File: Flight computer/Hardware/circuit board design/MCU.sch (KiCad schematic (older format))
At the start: 27 parts, among them J1 Conn_01x04, J2 Conn_01x02, J5 USB_B_Micro, U11 ATSAML21J18B-MUT, U7 W74M64FV, Y2 32.768KHz, Y3 16MHz

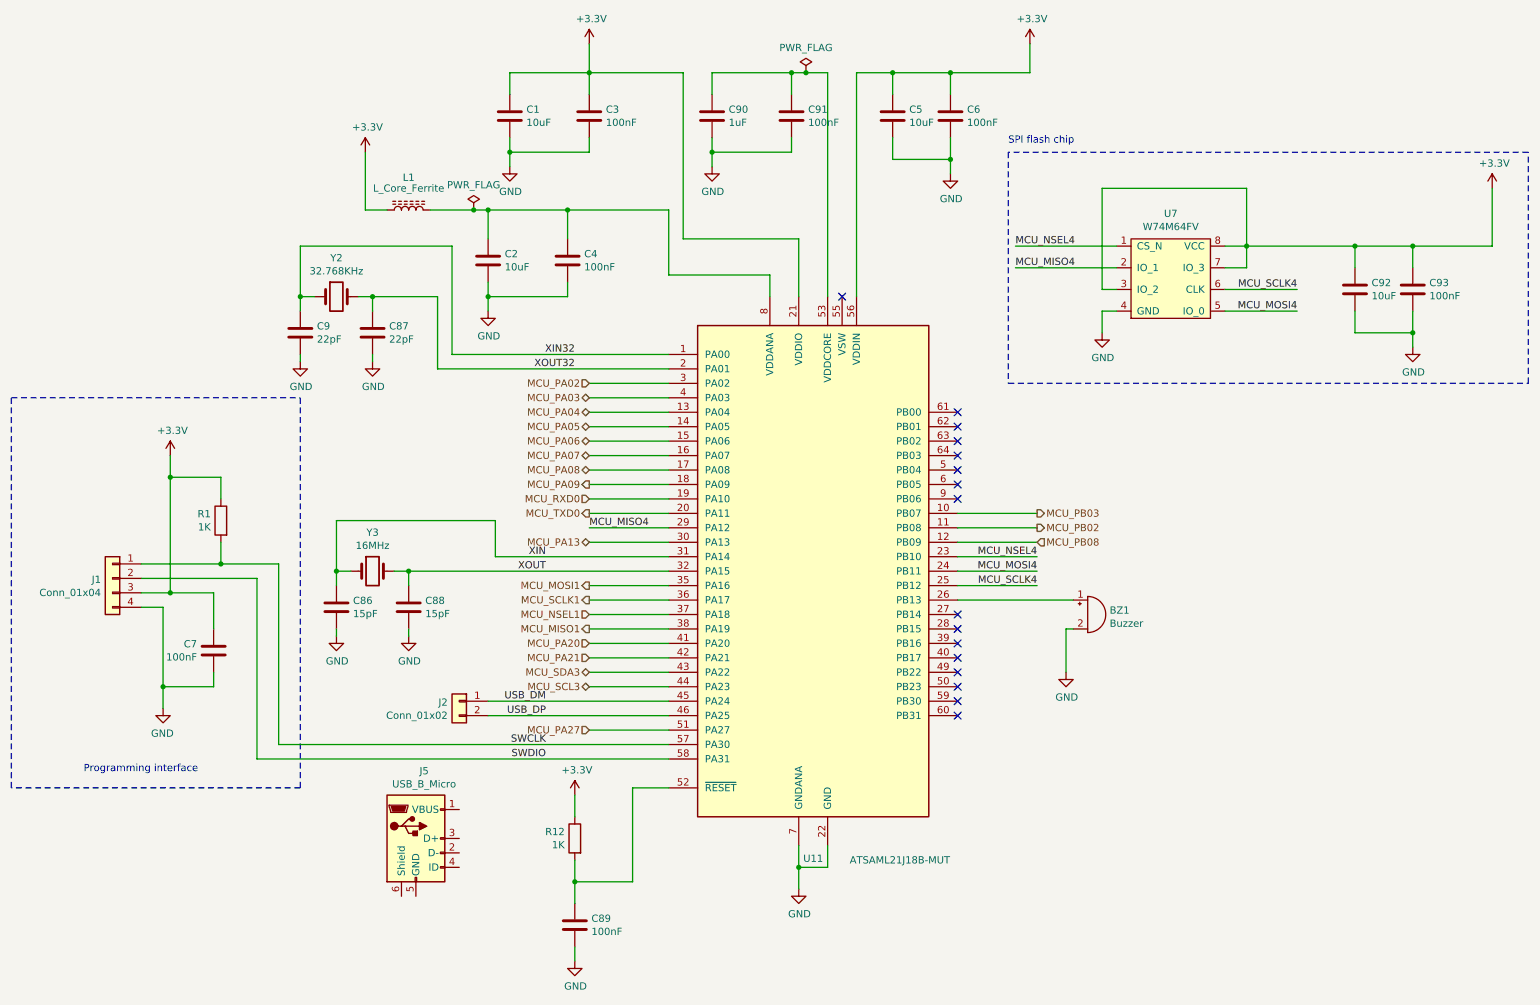
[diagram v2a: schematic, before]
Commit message: put in the IIS2MDC magnetometer
-fixed the error  spi connection pins for Flash chip
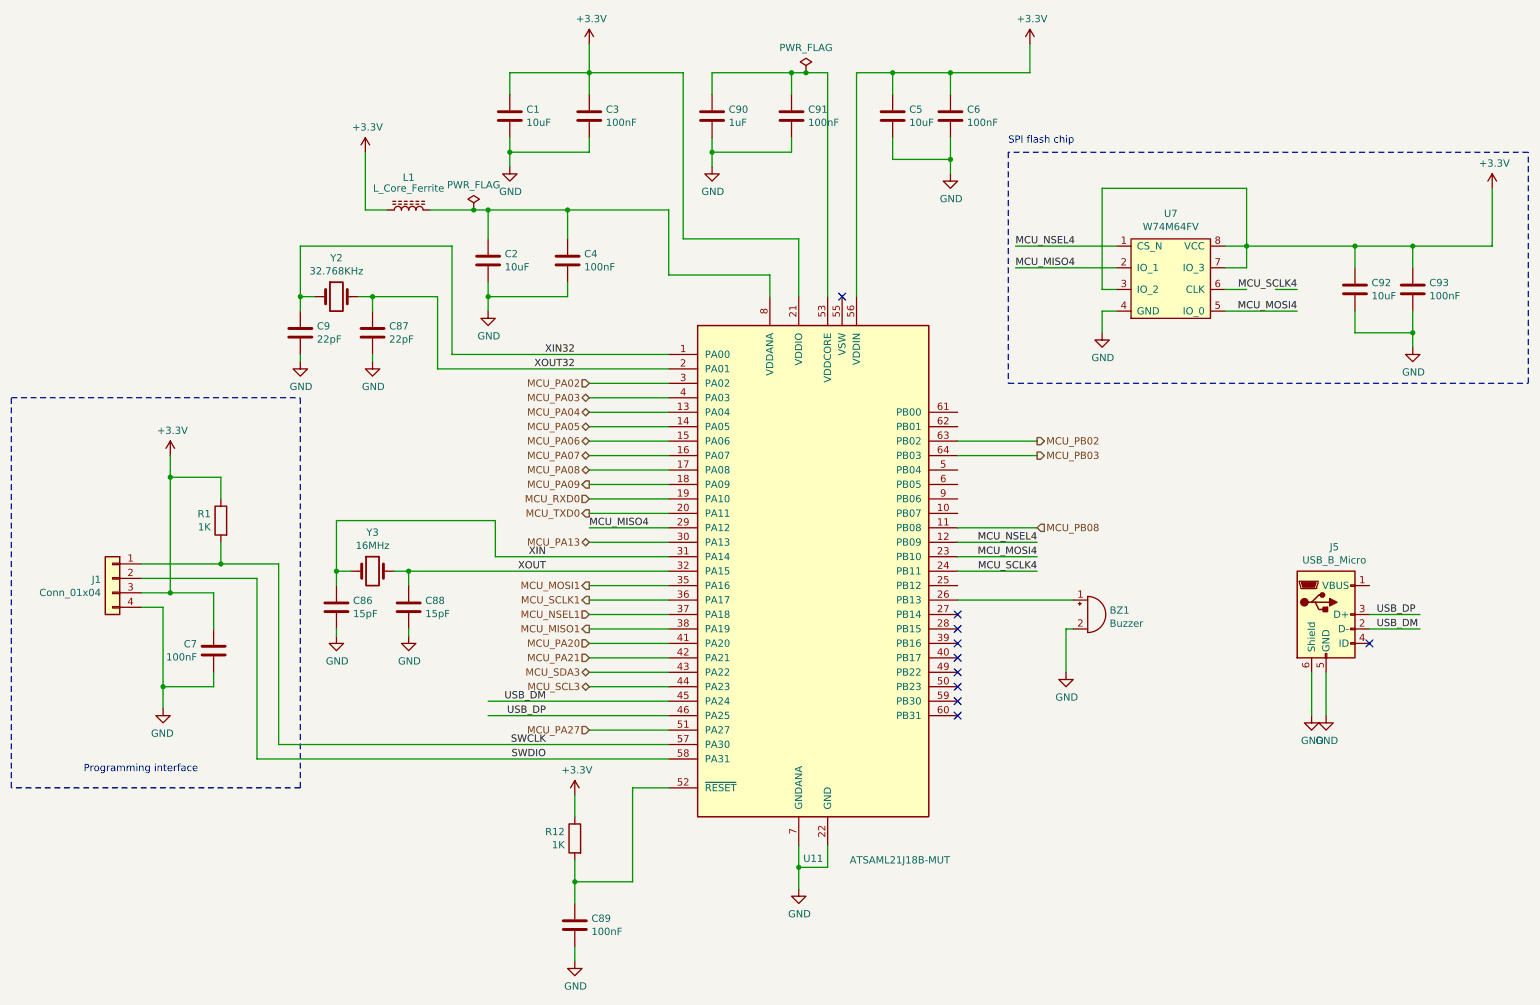
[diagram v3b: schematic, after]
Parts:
- removed J2: Conn_01x02, Connector_PinHeader_1.00mm:PinHeader_1x02_P1.00mm_Vertical, symbol Connector_Generic:Conn_01x02
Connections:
- wire segments 158 -> 163
- no-connect marks 16 -> 10
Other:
- moved on the sheet: J5
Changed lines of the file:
@@
 $Descr A4 11693 8268
 encoding utf-8
-Sheet 5 7
+Sheet 7 7
 Title ""
 Date ""
@@
 Wire Wire Line
 	4400 2400 4400 2500
-$Comp
-L Connector_Generic:Conn_01x02 J2
-U 1 1 5D2A0018
-P 3650 5300
-F 0 "J2" H 3730 5292 50  0000 L CNN
-F 1 "Conn_01x02" H 3730 5201 50  0000 L CNN
-F 2 "Connector_PinHeader_1.00mm:PinHeader_1x02_P1.00mm_Vertical" H 3650 5300 50  0001 C CNN
-F 3 "~" H 3650 5300 50  0001 C CNN
-	1    3650 5300
-	-1   0    0    -1
-$EndComp
 Wire Wire Line
 	3450 1900 3750 1900
@@
 	8100 2600 8100 2750
 Wire Wire Line
-	7100 4400 7650 4400
-Wire Wire Line
-	7100 4500 7650 4500
-Wire Wire Line
 	5100 3200 4550 3200
 Wire Wire Line
@@
 MCU_PA09
 Wire Wire Line
-	7100 4000 7650 4000
-Wire Wire Line
-	7100 4100 7650 4100
-Wire Wire Line
-	7100 4200 7650 4200
+	7100 3500 7650 3500
 Wire Wire Line
 	8100 1750 9100 1750
@@
 Wire Wire Line
 	9100 2300 9100 2150
+Text Label 7650 4300 2    50   ~ 0
+MCU_MOSI4
 Text Label 7650 4400 2    50   ~ 0
-MCU_MOSI4
-Text Label 7650 4500 2    50   ~ 0
 MCU_SCLK4
 Text Label 9450 2450 2    50   ~ 0
@@
 	9100 2150 9850 2150
 Wire Wire Line
-	8950 2450 9450 2450
+	8950 2450 9100 2450
 Wire Wire Line
 	8200 2150 7500 2150
@@
 MCU_PA13
 NoConn ~ 7100 4700
-Text HLabel 7650 4000 2    50   Output ~ 0
-MCU_PB03
-Text HLabel 7650 4100 2    50   Output ~ 0
+Text HLabel 7650 3500 2    50   Output ~ 0
 MCU_PB02
-Text HLabel 7650 4200 2    50   Input ~ 0
+Text HLabel 7650 4100 2    50   Input ~ 0
 MCU_PB08
-Wire Wire Line
-	7100 4300 7650 4300
-Text Label 7650 4300 2    50   ~ 0
-MCU_NSEL4
 Text Label 4550 4100 0    50   ~ 0
 MCU_MISO4
@@
 	1    0    0    -1
 $EndComp
-Wire Wire Line
-	7100 4600 7900 4600
 $Comp
 L power:GND #PWR021
@@
 NoConn ~ 7100 4900
 NoConn ~ 7100 4800
-NoConn ~ 7100 3900
-NoConn ~ 7100 3800
-NoConn ~ 7100 3700
-NoConn ~ 7100 3600
-NoConn ~ 7100 3500
-NoConn ~ 7100 3400
-NoConn ~ 7100 3300
 $Comp
 L Connector:USB_B_Micro J5
 U 1 1 5D7395BE
-P 3350 6250
-F 0 "J5" H 3407 6717 50  0000 C CNN
-F 1 "USB_B_Micro" H 3407 6626 50  0000 C CNN
-F 2 "" H 3500 6200 50  0001 C CNN
-F 3 "~" H 3500 6200 50  0001 C CNN
-	1    3350 6250
+P 9650 4700
+F 0 "J5" H 9707 5167 50  0000 C CNN
+F 1 "USB_B_Micro" H 9707 5076 50  0000 C CNN
+F 2 "" H 9800 4650 50  0001 C CNN
+F 3 "~" H 9800 4650 50  0001 C CNN
+	1    9650 4700
 	1    0    0    -1
 $EndComp
@@
 Text Notes 7450 1450 0    50   ~ 0
 SPI flash chip
+$Comp
+L power:GND #PWR0103
+U 1 1 5D7AB0A9
+P 9650 5400
+F 0 "#PWR0103" H 9650 5150 50  0001 C CNN
+F 1 "GND" H 9655 5227 50  0000 C CNN
+F 2 "" H 9650 5400 50  0001 C CNN
+F 3 "" H 9650 5400 50  0001 C CNN
+	1    9650 5400
+	1    0    0    -1
+$EndComp
+Text Label 10000 4800 0    50   ~ 0
+USB_DM
+Wire Wire Line
+	9950 4800 10300 4800
+Wire Wire Line
+	10300 4700 9950 4700
+Wire Wire Line
+	9650 5100 9650 5400
+$Comp
+L power:GND #PWR0104
+U 1 1 5D7F3C59
+P 9550 5400
+F 0 "#PWR0104" H 9550 5150 50  0001 C CNN
+F 1 "GND" H 9555 5227 50  0000 C CNN
+F 2 "" H 9550 5400 50  0001 C CNN
+F 3 "" H 9550 5400 50  0001 C CNN
+	1    9550 5400
+	1    0    0    -1
+$EndComp
+Wire Wire Line
+	9550 5100 9550 5400
+Text Label 10000 4700 0    50   ~ 0
+USB_DP
+NoConn ~ 9950 4900
+Wire Wire Line
+	9300 2450 9450 2450
+Text HLabel 7650 3600 2    50   Output ~ 0
+MCU_PB03
+Wire Wire Line
+	7100 3600 7650 3600
+Text Label 7650 4200 2    50   ~ 0
+MCU_NSEL4
+Wire Wire Line
+	7100 4100 7650 4100
+Wire Wire Line
+	7100 4200 7650 4200
+Wire Wire Line
+	7100 4300 7650 4300
+Wire Wire Line
+	7100 4400 7650 4400
+Wire Wire Line
+	7100 4600 7900 4600
 $EndSCHEMATC

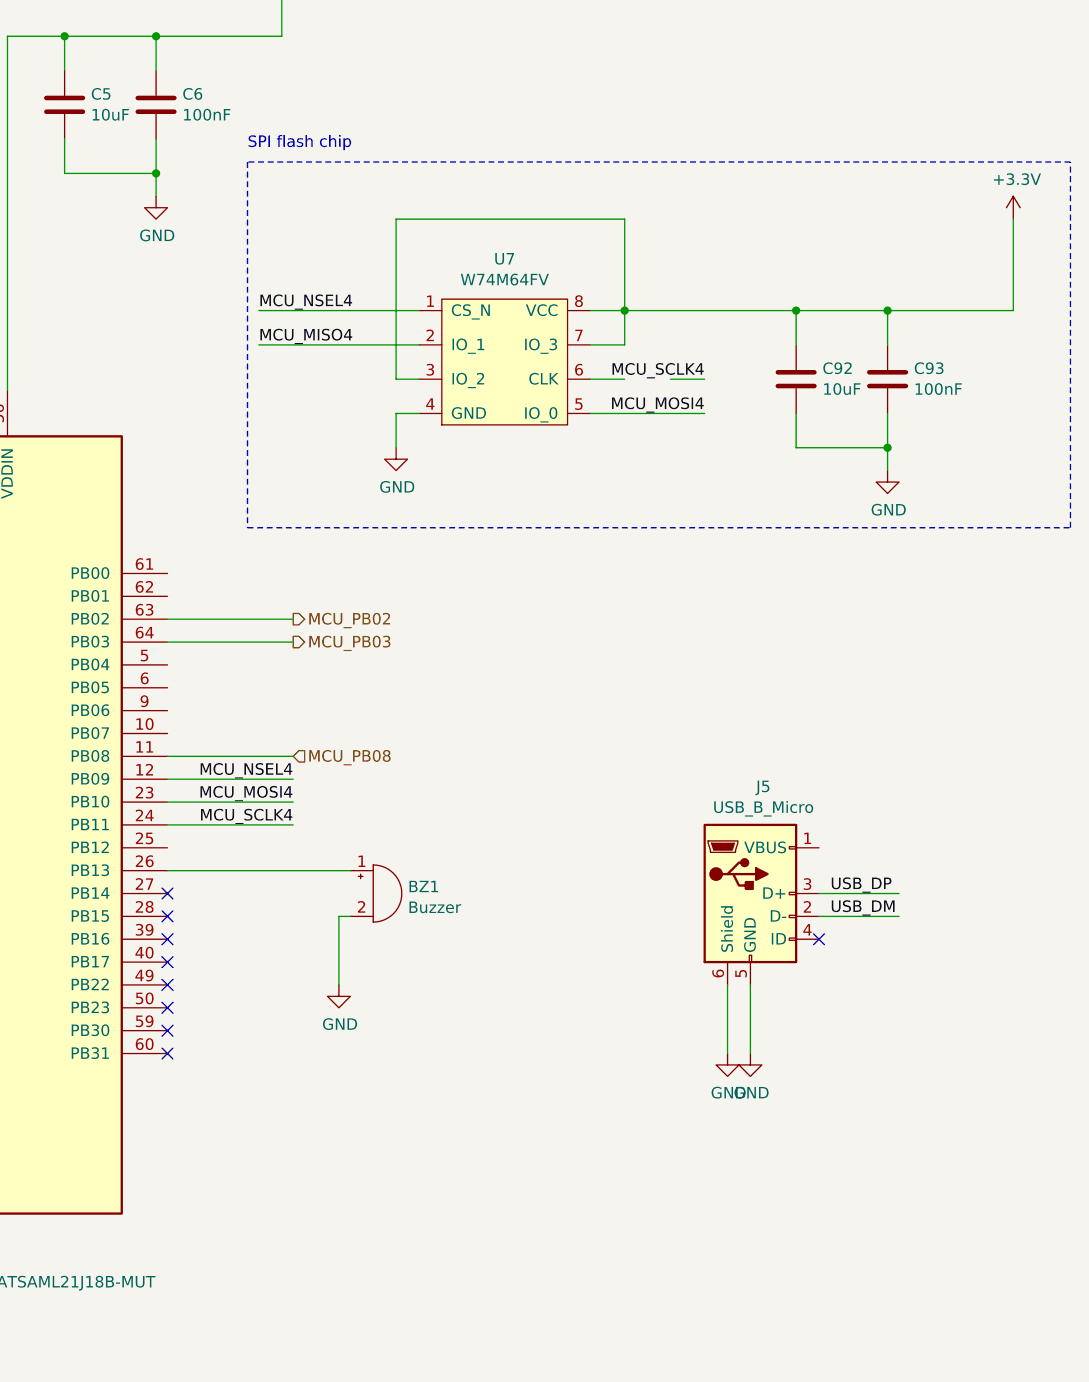
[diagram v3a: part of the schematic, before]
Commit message: Wired up the FETs
-fixed the ERC error for the BMI088 symbol
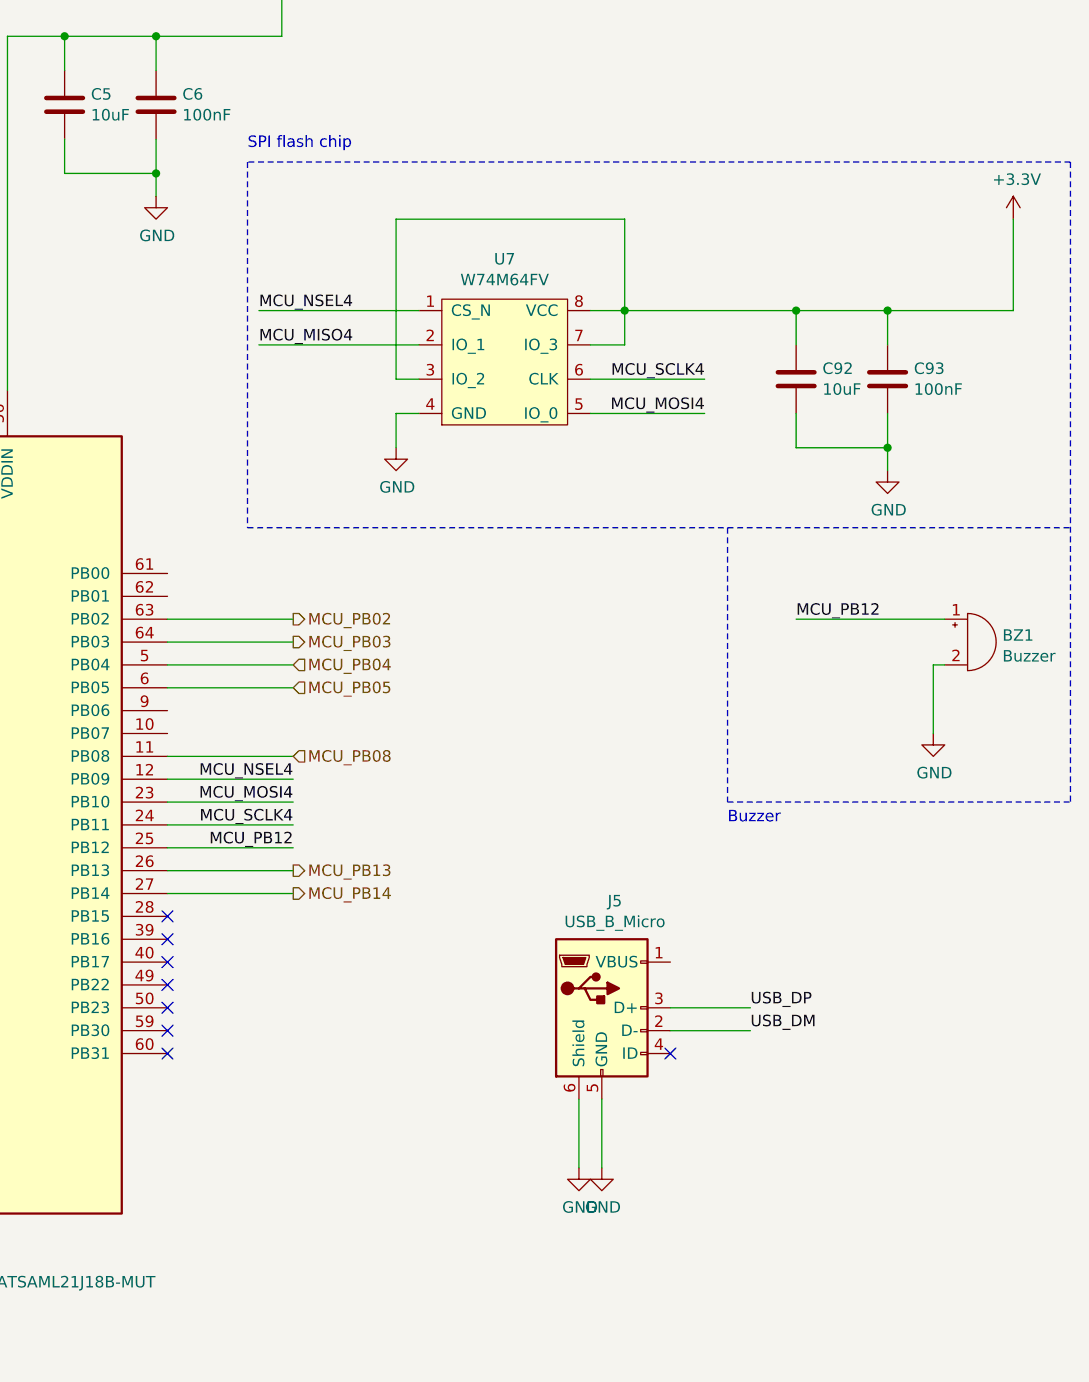
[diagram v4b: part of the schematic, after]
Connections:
- net labels added: MCU_PB04, MCU_PB05, MCU_PB12, MCU_PB13, MCU_PB14
- wire segments 163 -> 167
- no-connect marks 10 -> 9
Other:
- note added: "Buzzer\n"
- moved on the sheet: BZ1, J5
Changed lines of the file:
@@
 	9100 2150 9850 2150
-Wire Wire Line
-	8950 2450 9100 2450
 Wire Wire Line
 	8200 2150 7500 2150
@@
 Text HLabel 4550 4200 0    50   BiDi ~ 0
 MCU_PA13
-NoConn ~ 7100 4700
 Text HLabel 7650 3500 2    50   Output ~ 0
 MCU_PB02
@@
 L Device:Buzzer BZ1
 U 1 1 5D650F14
-P 8000 4700
-F 0 "BZ1" H 8152 4729 50  0000 L CNN
-F 1 "Buzzer" H 8152 4638 50  0000 L CNN
-F 2 "Buzzer_Beeper:Buzzer_12x9.5RM7.6" V 7975 4800 50  0001 C CNN
-F 3 "https://docs-emea.rs-online.com/webdocs/1581/0900766b815810c5.pdf" V 7975 4800 50  0001 C CNN
-F 4 "1.05" H 8000 4700 50  0001 C CNN "Cost"
-F 5 "https://uk.rs-online.com/web/p/magnetic-buzzer-components/6173081/?searchTerm=6173081&relevancy-data=636F3D3126696E3D4931384E525353746F636B4E756D6265724D504E266C753D656E266D6D3D6D61746368616C6C26706D3D5E5C647B367D247C5E5C647B377D247C5E5C647B31307D2426706F3D313426736E3D592673743D52535F53544F434B5F4E554D4245522677633D4E4F4E45267573743D3631373330383126" H 8000 4700 50  0001 C CNN "Purchase link"
-	1    8000 4700
+P 10600 3600
+F 0 "BZ1" H 10752 3629 50  0000 L CNN
+F 1 "Buzzer" H 10752 3538 50  0000 L CNN
+F 2 "Buzzer_Beeper:Buzzer_12x9.5RM7.6" V 10575 3700 50  0001 C CNN
+F 3 "https://docs-emea.rs-online.com/webdocs/1581/0900766b815810c5.pdf" V 10575 3700 50  0001 C CNN
+F 4 "1.05" H 10600 3600 50  0001 C CNN "Cost"
+F 5 "https://uk.rs-online.com/web/p/magnetic-buzzer-components/6173081/?searchTerm=6173081&relevancy-data=636F3D3126696E3D4931384E525353746F636B4E756D6265724D504E266C753D656E266D6D3D6D61746368616C6C26706D3D5E5C647B367D247C5E5C647B377D247C5E5C647B31307D2426706F3D313426736E3D592673743D52535F53544F434B5F4E554D4245522677633D4E4F4E45267573743D3631373330383126" H 10600 3600 50  0001 C CNN "Purchase link"
+	1    10600 3600
 	1    0    0    -1
 $EndComp
@@
 L power:GND #PWR021
 U 1 1 5D659D89
-P 7850 5100
-F 0 "#PWR021" H 7850 4850 50  0001 C CNN
-F 1 "GND" H 7855 4927 50  0000 C CNN
-F 2 "" H 7850 5100 50  0001 C CNN
-F 3 "" H 7850 5100 50  0001 C CNN
-	1    7850 5100
-	1    0    0    -1
-$EndComp
-Wire Wire Line
-	7850 5100 7850 4800
-Wire Wire Line
-	7850 4800 7900 4800
+P 10450 4000
+F 0 "#PWR021" H 10450 3750 50  0001 C CNN
+F 1 "GND" H 10455 3827 50  0000 C CNN
+F 2 "" H 10450 4000 50  0001 C CNN
+F 3 "" H 10450 4000 50  0001 C CNN
+	1    10450 4000
+	1    0    0    -1
+$EndComp
+Wire Wire Line
+	10450 4000 10450 3700
+Wire Wire Line
+	10450 3700 10500 3700
 $Comp
 L power:+3.3V #PWR022
@@
 NoConn ~ 7100 4900
 NoConn ~ 7100 4800
-$Comp
-L Connector:USB_B_Micro J5
-U 1 1 5D7395BE
-P 9650 4700
-F 0 "J5" H 9707 5167 50  0000 C CNN
-F 1 "USB_B_Micro" H 9707 5076 50  0000 C CNN
-F 2 "" H 9800 4650 50  0001 C CNN
-F 3 "~" H 9800 4650 50  0001 C CNN
-	1    9650 4700
-	1    0    0    -1
-$EndComp
 Wire Notes Line
 	7450 1500 7450 3100
 Wire Notes Line
 	7450 3100 11050 3100
-Wire Notes Line
-	11050 3100 11050 1500
 Wire Notes Line
 	11050 1500 7450 1500
 Text Notes 7450 1450 0    50   ~ 0
 SPI flash chip
-$Comp
-L power:GND #PWR0103
-U 1 1 5D7AB0A9
-P 9650 5400
-F 0 "#PWR0103" H 9650 5150 50  0001 C CNN
-F 1 "GND" H 9655 5227 50  0000 C CNN
-F 2 "" H 9650 5400 50  0001 C CNN
-F 3 "" H 9650 5400 50  0001 C CNN
-	1    9650 5400
-	1    0    0    -1
-$EndComp
-Text Label 10000 4800 0    50   ~ 0
+Text Label 9650 5300 0    50   ~ 0
 USB_DM
-Wire Wire Line
-	9950 4800 10300 4800
-Wire Wire Line
-	10300 4700 9950 4700
-Wire Wire Line
-	9650 5100 9650 5400
-$Comp
-L power:GND #PWR0104
-U 1 1 5D7F3C59
-P 9550 5400
-F 0 "#PWR0104" H 9550 5150 50  0001 C CNN
-F 1 "GND" H 9555 5227 50  0000 C CNN
-F 2 "" H 9550 5400 50  0001 C CNN
-F 3 "" H 9550 5400 50  0001 C CNN
-	1    9550 5400
-	1    0    0    -1
-$EndComp
-Wire Wire Line
-	9550 5100 9550 5400
-Text Label 10000 4700 0    50   ~ 0
+Text Label 9650 5200 0    50   ~ 0
 USB_DP
-NoConn ~ 9950 4900
-Wire Wire Line
-	9300 2450 9450 2450
 Text HLabel 7650 3600 2    50   Output ~ 0
 MCU_PB03
@@
 	7100 4300 7650 4300
 Wire Wire Line
-	7100 4400 7650 4400
-Wire Wire Line
-	7100 4600 7900 4600
+	8950 2450 9450 2450
+Wire Wire Line
+	7650 4400 7100 4400
+NoConn ~ 9300 5400
+Wire Wire Line
+	8900 5600 8900 5900
+$Comp
+L power:GND #PWR0104
+U 1 1 5D7F3C59
+P 8900 5900
+F 0 "#PWR0104" H 8900 5650 50  0001 C CNN
+F 1 "GND" H 8905 5727 50  0000 C CNN
+F 2 "" H 8900 5900 50  0001 C CNN
+F 3 "" H 8900 5900 50  0001 C CNN
+	1    8900 5900
+	1    0    0    -1
+$EndComp
+Wire Wire Line
+	9000 5600 9000 5900
+Wire Wire Line
+	9650 5200 9300 5200
+Wire Wire Line
+	9300 5300 9650 5300
+$Comp
+L power:GND #PWR0103
+U 1 1 5D7AB0A9
+P 9000 5900
+F 0 "#PWR0103" H 9000 5650 50  0001 C CNN
+F 1 "GND" H 9005 5727 50  0000 C CNN
+F 2 "" H 9000 5900 50  0001 C CNN
+F 3 "" H 9000 5900 50  0001 C CNN
+	1    9000 5900
+	1    0    0    -1
+$EndComp
+$Comp
+L Connector:USB_B_Micro J5
+U 1 1 5D7395BE
+P 9000 5200
+F 0 "J5" H 9057 5667 50  0000 C CNN
+F 1 "USB_B_Micro" H 9057 5576 50  0000 C CNN
+F 2 "" H 9150 5150 50  0001 C CNN
+F 3 "~" H 9150 5150 50  0001 C CNN
+	1    9000 5200
+	1    0    0    -1
+$EndComp
+Wire Wire Line
+	7650 4500 7100 4500
+Text Label 9850 3500 0    50   ~ 0
+MCU_PB12
+Wire Wire Line
+	9850 3500 10500 3500
+Text Label 7650 4500 2    50   ~ 0
+MCU_PB12
+Wire Notes Line
+	9550 4300 11050 4300
+Wire Notes Line
+	11050 1500 11050 4300
+Wire Notes Line
+	9550 3100 9550 4300
+Text Notes 9550 4400 0    50   ~ 0
+Buzzer\n
+Wire Wire Line
+	7100 3700 7650 3700
+Wire Wire Line
+	7100 3800 7650 3800
+Text HLabel 7650 3700 2    50   Input ~ 0
+MCU_PB04
+Text HLabel 7650 3800 2    50   Input ~ 0
+MCU_PB05
+Wire Wire Line
+	7100 4600 7650 4600
+Wire Wire Line
+	7100 4700 7650 4700
+Text HLabel 7650 4600 2    50   Output ~ 0
+MCU_PB13
+Text HLabel 7650 4700 2    50   Output ~ 0
+MCU_PB14
 $EndSCHEMATC
